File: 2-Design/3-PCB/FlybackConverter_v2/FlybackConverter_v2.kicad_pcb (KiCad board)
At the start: 2 copper layers, 120 x 40 mm, 56 parts, among them U1 TL431DBZ, U2 LM7812_TO220

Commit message: Gate loop is not long anymore. Still, why not be sad :(.
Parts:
- CA1: value C -> 1n
- CF1: value C -> 20p
- CP1: value C -> NAN
- CS1: value C -> 10n
- CSnubber1: value C -> 4.7u-2220-50V
- CT1: value C -> 0.72n
- CZ1: value C -> 20n
- DSnubber1: value MBRA340 -> M3/5BT; footprint Diode_SMD:D_SMA -> Diode_SMD:D_SMB_Handsoldering
- FLYBACK_DIODE_SUBSTITUTE1: footprint Diode_SMD:D_SMC -> Diode_SMD:D_SMC_Handsoldering
- RA1, RF1, RJ1, RP1: value R -> 10k
- RAC1, RE1: value R -> 1k
- RB1, RC1, RK1: value R -> 4.7k
- RCS1: value R -> 10m
- RG1: value R -> 10
- RG2, RZ1: value R -> 22k
- RI1: value R -> 85k
- RS1: value R -> 330k
- RS2: value R -> 2.2k
- RSnubber1: value R -> 82//82
- RT1: value 10 -> 12k
- moved TestPointB2 32.4 mm to (54.1, 8.25)
- moved RS2 18.5 mm to (92.7, 37.7), turned to 0 degrees
- moved RS1 18.0 mm to (92.7, 35.6), turned to 180 degrees
- moved CF1 17.2 mm to (89.7, 36.8), turned to -90 degrees
- moved RP1 16.9 mm to (75.8, 30.4)
- moved CS1 16.0 mm to (91.2, 33.4), turned to 0 degrees
- moved RA1 12.7 mm to (82.2, 37.0), turned to 90 degrees
- moved RCS1 12.1 mm to (86.7, 24.2)
- moved TestPointB1 10.9 mm to (72.8, 37.4)
- moved RC1 10.8 mm to (76.6, 35.4)
- moved RB1 10.3 mm to (76.6, 37.6)
- moved CA1 9.97 mm to (79.8, 37.0), turned to 90 degrees
- moved RT1 9.73 mm to (81.4, 31.4), turned to 0 degrees
- moved CVREF1 9.09 mm to (78.0, 31.0), turned to -90 degrees
- moved CIN4 7.90 mm to (65.9, 23.2)
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- renumbered DC1 to D_Z_10V1, TVS1 to D_Z_15V1
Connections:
- RG2 pad 1: Net-(MOSFET1-Pad1) -> GND
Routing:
- net GND: track 103.6 -> 70.8 mm
- net Net-(CVREF1-Pad1): track 52.8 -> 28.5 mm, vias 2 -> 0
- net Net-(MOSFET1-Pad1): track 7.18 -> 23.9 mm, vias 2 -> 1
- net Net-(CF1-Pad1): track 39.8 -> 23.4 mm
- net Net-(CA1-Pad2): track 19.0 -> 5.80 mm, vias 1 -> 0
- net Net-(CA1-Pad1): track 17.7 -> 11.0 mm, vias 2 -> 0
- net Net-(MOSFET1-Pad4): track 0.00 -> 6.22 mm
- net Net-(PWMController1-Pad6): track 7.86 -> 2.54 mm
- net Net-(CS1-Pad1): track 16.5 -> 11.5 mm
- net Net-(OPTO1-Pad3): track 15.3 -> 19.6 mm
- net Net-(CVCC1-Pad2): track 69.8 -> 67.7 mm
- net Net-(CS1-Pad2): track 2.06 -> 3.21 mm
- added copper zone on F.Cu, net Net-(CF1-Pad1)
- added copper zone on F.Cu, net Net-(CVREF1-Pad1)
- removed copper zone on B.Cu, net Net-(MOSFET1-Pad1)
- removed copper zone on B.Cu, net Net-(MOSFET1-Pad4)
- removed copper zone on F.Cu, net Net-(MOSFET1-Pad4)

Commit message: [PCB] board update
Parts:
- added CSnubber2: 4.7u-2220-50V, Capacitor_SMD:C_1210_3225Metric_Pad1.33x2.70mm_HandSolder, F.Cu at (115.7, 28.0)
- added RG3: 0, Resistor_SMD:R_1206_3216Metric, F.Cu at (38.3, 30.1)
- added RSnubber2: 82//82, Resistor_SMD:R_2010_5025Metric_Pad1.40x2.65mm_HandSolder, F.Cu at (123.4, 28.9)
- CF1: value 20p -> 22p
- CZ1: value 20n -> 22n
- moved RSnubber1 7.72 mm to (119.6, 28.9), turned to -90 degrees
- moved RCS1 5.65 mm to (81.0, 24.2)
- moved OPTO1 2.00 mm to (60.0, 34.5)
- moved RF1 1.12 mm to (47.6, 34.7)
- moved COUT1 1.00 mm to (68.3, 47.1)
- moved DSnubber1 0.82 mm to (104.8, 27.8)
- moved CSnubber1 0.60 mm to (111.8, 28.0), turned to -90 degrees
- moved RE1 0.30 mm to (42.0, 36.0)
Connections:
- U2 pad 1: Net-(CIN1-Pad1) -> Net-(U2-Pad1)
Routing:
- net Net-(U2-Pad1): track 0.00 -> 11.3 mm
- net Net-(CIN1-Pad1): track 13.8 -> 3.56 mm
- net GND: track 70.8 -> 80.0 mm
- net Net-(MOSFET1-Pad1): track 23.9 -> 28.5 mm
- net Net-(OPTO1-Pad1): track 5.15 -> 8.56 mm
- net Net-(CVREF1-Pad1): track 28.5 -> 25.9 mm
- net Net-(CP1-Pad1): track 15.1 -> 17.3 mm
- net Net-(OPTO1-Pad3): track 19.6 -> 17.6 mm
- net Net-(D_Z_10V1-Pad1): track 8.71 -> 7.67 mm
- net Net-(MOSFET1-Pad4): track 6.22 -> 5.23 mm
- net Net-(CVCC1-Pad2): vias 2 -> 0
- added copper zone on F.Cu, net Net-(D_Z_10V1-Pad1)
- added copper zone on B.Cu, net Net-(MOSFET1-Pad1)
- removed copper zone on B.Cu, net Net-(CSnubber1-Pad2)

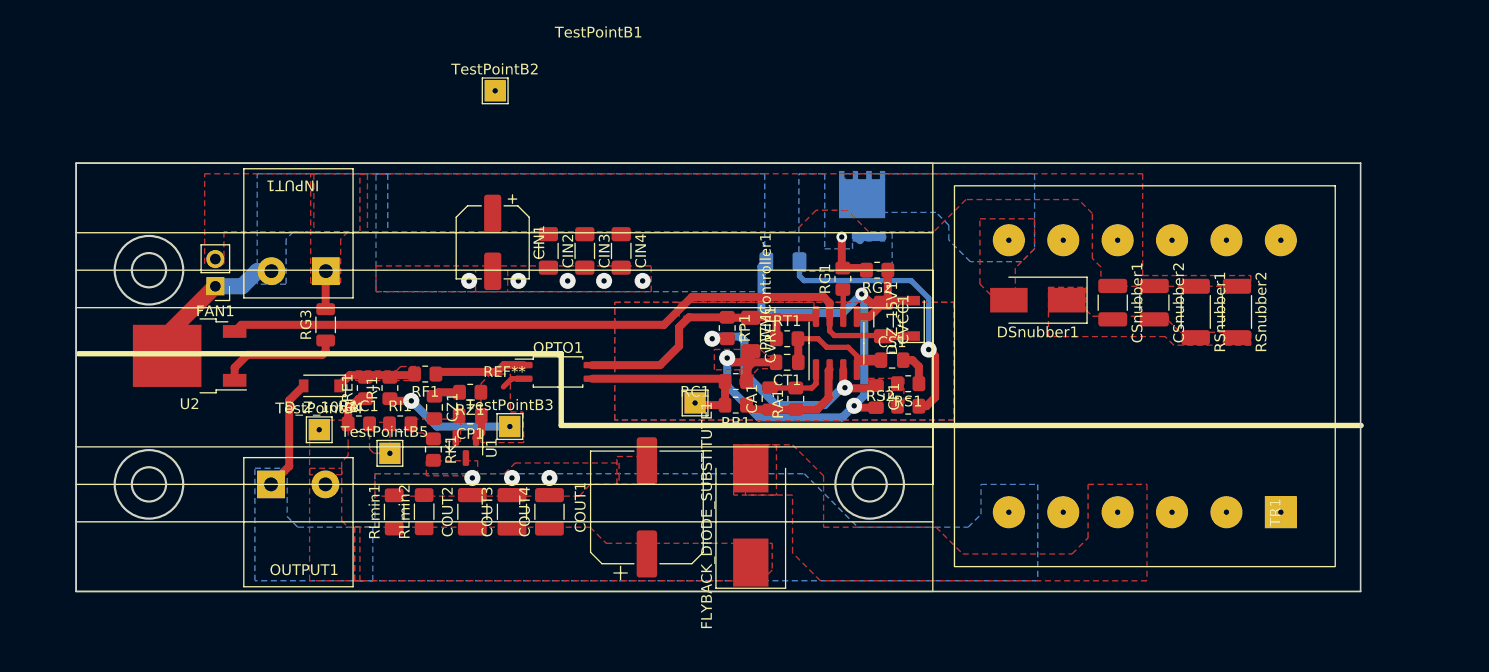
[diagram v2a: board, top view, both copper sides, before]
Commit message: [PCB] snubber resistor change
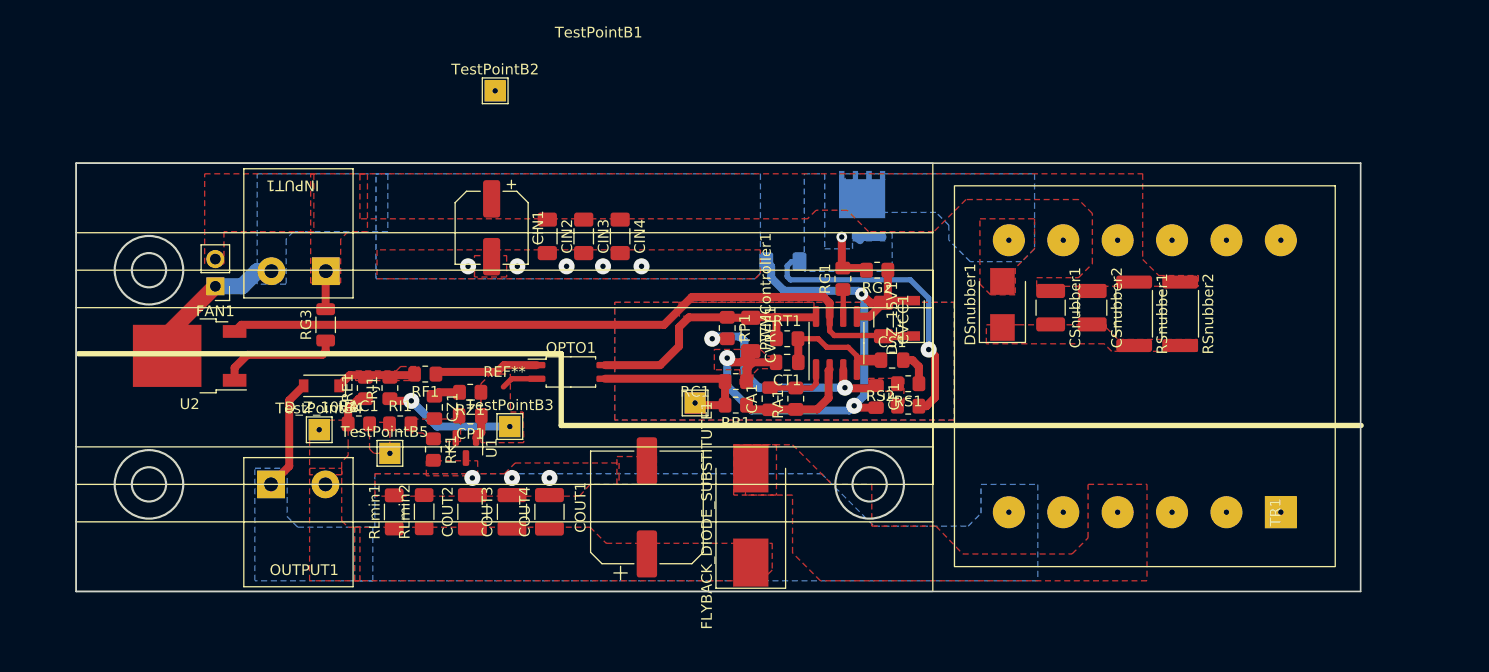
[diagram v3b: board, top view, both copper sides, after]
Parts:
- DSnubber1: footprint Diode_SMD:D_SMB_Handsoldering -> Diode_SMD:D_SMB
- RSnubber1, RSnubber2: footprint Resistor_SMD:R_2010_5025Metric_Pad1.40x2.65mm_HandSolder -> Resistor_SMD:R_2512_6332Metric
- moved CSnubber1 5.82 mm to (106.0, 28.5)
- moved CSnubber2 5.82 mm to (109.9, 28.5)
- moved RSnubber1 5.76 mm to (113.8, 29.1)
- moved RSnubber2 5.30 mm to (118.1, 29.1)
- moved DSnubber1 3.32 mm to (101.5, 28.2), turned to 90 degrees
- moved CIN4 1.37 mm to (65.8, 21.8)
- moved CIN2 1.37 mm to (59.0, 21.8)
- moved CIN3 1.37 mm to (62.4, 21.8)
- moved CIN1 1.37 mm to (53.8, 21.0)
- moved OPTO1 1.20 mm to (61.2, 34.5)
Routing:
- net GND: track 80.0 -> 75.1 mm
- net Net-(MOSFET1-Pad1): track 28.5 -> 30.6 mm
- net Net-(CF1-Pad1): track 23.4 -> 22.1 mm
- net Net-(OPTO1-Pad1): track 8.56 -> 9.76 mm
- net Net-(CVREF1-Pad1): track 25.9 -> 24.7 mm
- net Net-(CP1-Pad1): track 17.3 -> 18.5 mm
- net Net-(OPTO1-Pad3): track 17.6 -> 16.4 mm

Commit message: [PCB] last corrections and cillibom
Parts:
- removed TestPointB2: Conn_01x01_Female, kutup:TestPoint_THTPad_2.0x2.0mm_Drill1.0mm
- added COUT5: 100nF, Capacitor_SMD:C_1206_3216Metric, F.Cu at (79.0, 52.8)
- added G***: LOGO, kutup:mind-the-cap-small, F.Cu at (120.8, 38.8)
- added G***: LOGO, kutup:mind-the-cap-small, F.Cu at (105.2, 38.8)
- added RES1: 1k, Resistor_SMD:R_2512_6332Metric, F.Cu at (80.2, 47.8)
- FLYBACK_DIODE_SUBSTITUTE1: footprint Diode_SMD:D_SMC_Handsoldering -> Diode_SMD:D_SMC
- RE1: value 1k -> 2.2k
- moved CIN4 10.1 mm to (75.9, 21.8)
- moved CIN3 10.1 mm to (72.5, 21.8)
- moved CIN2 10.1 mm to (69.1, 21.8)
- moved CIN1 6.55 mm to (47.2, 21.0)
- moved FLYBACK_DIODE_SUBSTITUTE1 3.75 mm to (74.2, 47.9)
- moved COUT1 3.41 mm to (65.0, 48.0)
- moved COUT2 1.50 mm to (50.5, 47.6)
- moved COUT3 1.50 mm to (54.2, 47.6)
- moved COUT4 1.50 mm to (57.7, 47.6)
- moved TestPointB1 1.40 mm to (72.8, 36.0)
- moved RSnubber1 0.82 mm to (113.8, 28.2)
- moved RSnubber2 0.82 mm to (118.1, 28.2)
- moved RG3 0.10 mm to (38.2, 30.1)
- moved TestPointB4 0.10 mm to (37.8, 39.9)
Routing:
- net Net-(COUT1-Pad1): track 3.36 -> 8.56 mm
- net GNDREF: track 10.5 -> 6.51 mm, vias 3 -> 4
- net Net-(RES1-Pad2): track 0.00 -> 3.73 mm
- net GND: track 75.1 -> 78.2 mm, vias 8 -> 12
- net Net-(OPTO1-Pad3): track 16.4 -> 14.4 mm
- net (no net): track 0.00 -> 1.50 mm
- net Net-(RG3-Pad1): track 11.3 -> 10.6 mm
- net Net-(CIN1-Pad1): track 3.56 -> 3.66 mm, vias 0 -> 1
- added copper zone on B.Cu, net Net-(CIN1-Pad1)
- added copper zone on F.Cu, net Net-(RES1-Pad2)
